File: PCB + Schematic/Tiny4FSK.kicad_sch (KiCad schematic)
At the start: 83 parts, among them J1 Power Ext, J2 GPIO, J3 I2C, J4 USB, J5 USB Breakout, J6 SPI, J7 USBC, J8 SWD, SW1 Power Switch, SW1 RST, U1 ATSAMD21G18A-A, U2 ATGM336H, U2 TPS61200DRC, U4 ECS-327TXO-2012, U6 SI4063, U7 Linear Step-Down

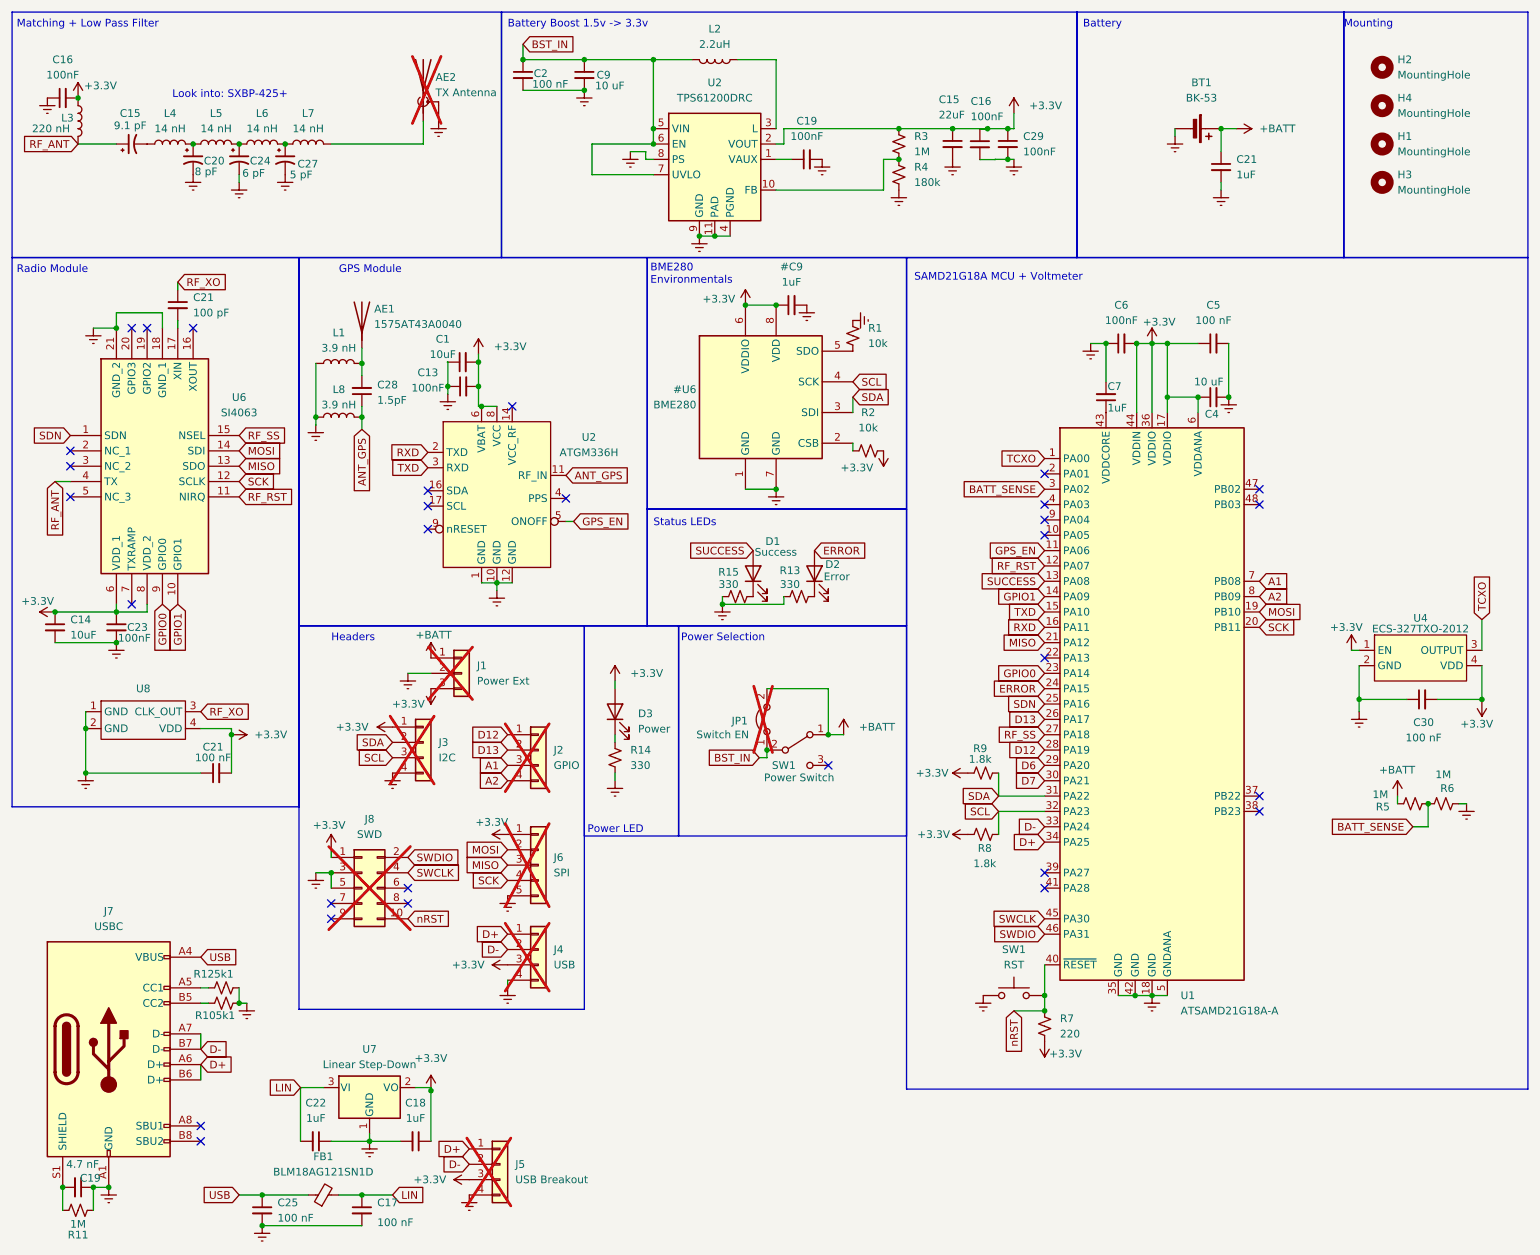
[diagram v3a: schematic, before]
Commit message: small updates to PCB, revamp README
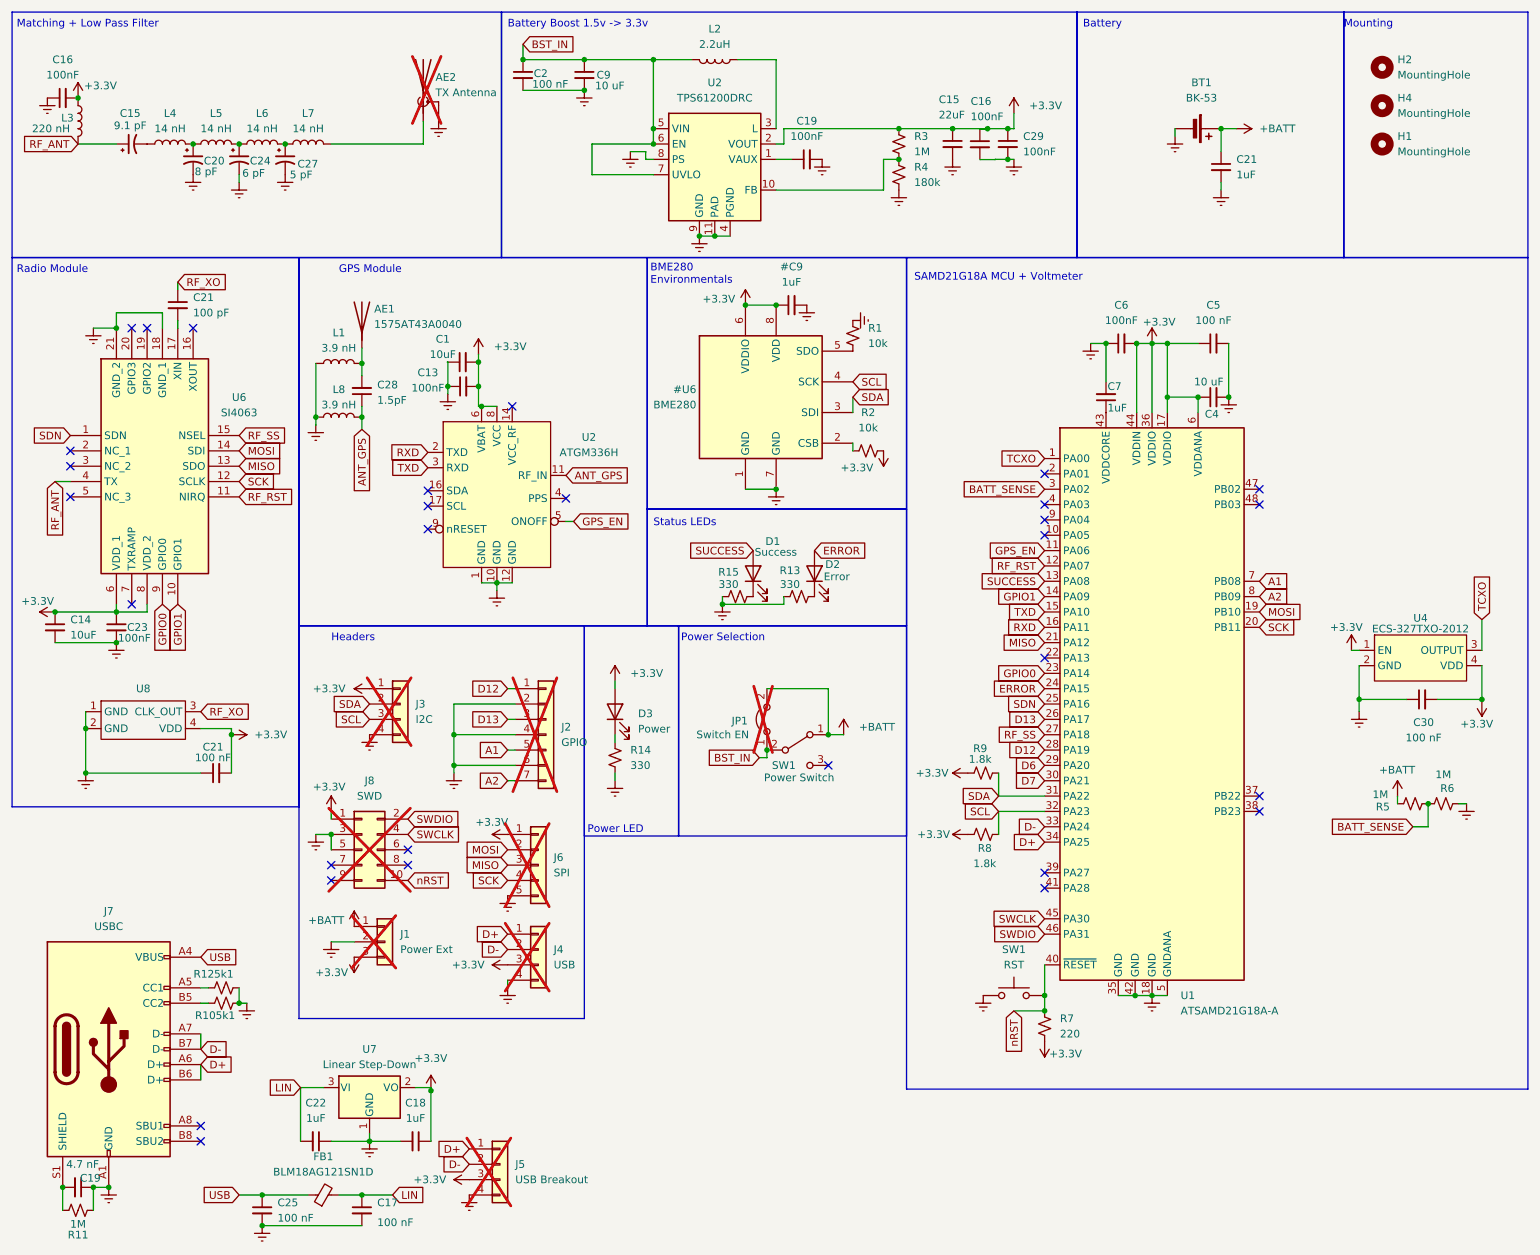
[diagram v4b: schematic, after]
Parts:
- removed H3: MountingHole, MountingHole:MountingHole_2.2mm_M2, symbol Mechanical:MountingHole
- removed J2: GPIO, Connector_PinHeader_2.54mm:PinHeader_1x04_P2.54mm_Vertical, symbol Connector_Generic:Conn_01x04
- added J2: GPIO, Connector_PinHeader_2.54mm:PinHeader_1x07_P2.54mm_Vertical, symbol Connector_Generic:Conn_01x07
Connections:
- net A1: now also J2.5 (Pin_5)
- net A2: now also J2.7 (Pin_7)
- net D12: now also J2.1 (Pin_1)
- net D13: now also J2.3 (Pin_3)
- net Earth: now also J2.2 (Pin_2), J2.4 (Pin_4), J2.6 (Pin_6)
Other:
- note removed: "Look into: SXBP-425+"
- moved on the sheet: J1, J3, J8

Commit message: Refactor Tiny4FSK project files and add shield functionality
- Updated Tiny4FSK.kicad_pro to include layer_pairs and changed the 3D model reference to Tiny4FSK-simple.step.
- Modified Tiny4FSK.kicad_sch to replace a 7-pin connector with a 9-pin connector, adjusting pin positions and properties accordingly.
- Introduced new shield.cpp and shield.h files to support interaction with the Tiny4FSK General Shield, including I2C scanning and initialization for BME280, IMU, and OLED devices.
- Added a new 3D model file Tiny4FSK-simple.step.
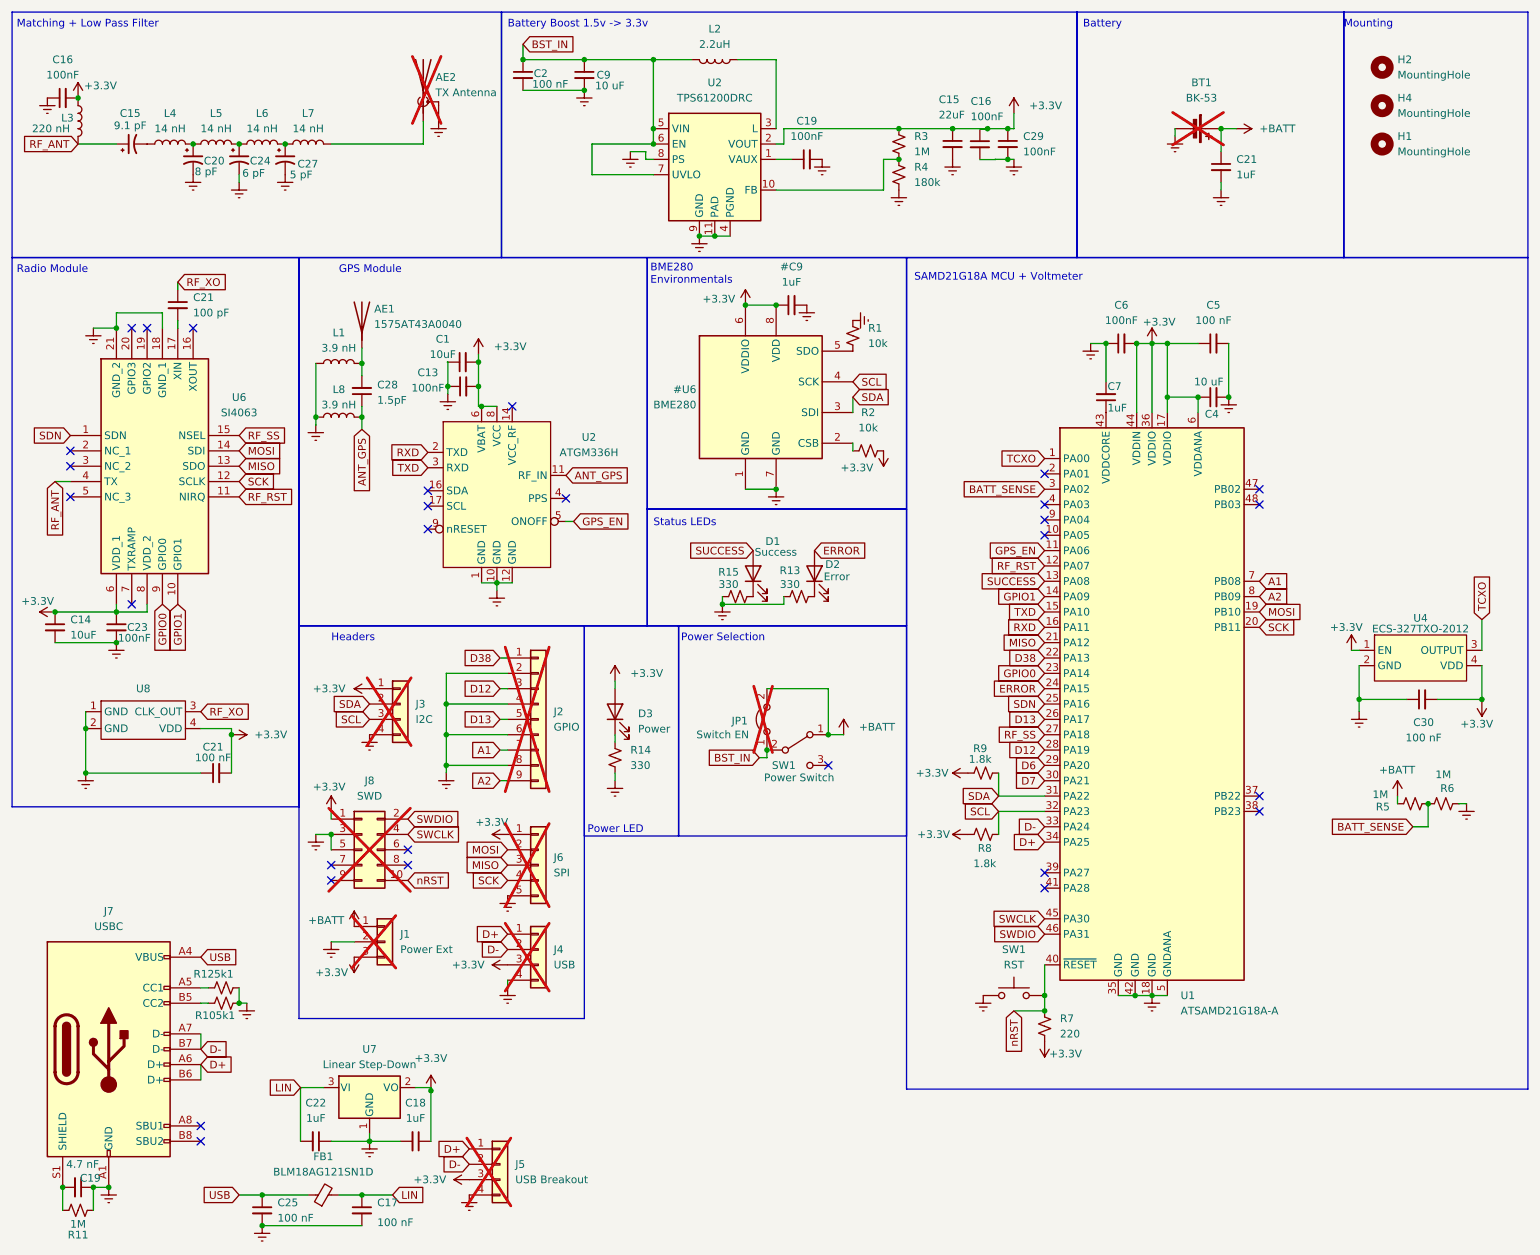
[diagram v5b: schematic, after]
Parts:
- BT1: now not fitted
- J2: footprint Connector_PinHeader_2.54mm:PinHeader_1x07_P2.54mm_Vertical -> Connector_PinHeader_2.54mm:PinHeader_1x09_P2.54mm_Vertical; symbol Connector_Generic:Conn_01x07 -> Connector_Generic:Conn_01x09
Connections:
- net A1: now also J2.7 (Pin_7); no longer J2.5 (Pin_5)
- net A2: now also J2.9 (Pin_9); no longer J2.7 (Pin_7)
- net D12: now also J2.3 (Pin_3); no longer J2.1 (Pin_1)
- net D13: now also J2.5 (Pin_5); no longer J2.3 (Pin_3)
- net Earth: now also J2.8 (Pin_8)
- net D38: now reaches U1.22 (PA13)
- net D38: now also J2.1 (Pin_1)
- no-connect marks 30 -> 29

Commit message: new production files
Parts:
- U4: footprint Oscillator_TCXO:ECS-327TXO-2012 -> Crystal:Crystal_SMD_3225-4Pin_3.2x2.5mm
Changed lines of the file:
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@@
 			)
 		)
-		(property "Footprint" "Oscillator_TCXO:ECS-327TXO-2012"
+		(property "Footprint" "Crystal:Crystal_SMD_3225-4Pin_3.2x2.5mm"
 			(at 247.65 118.11 0)
 			(effects

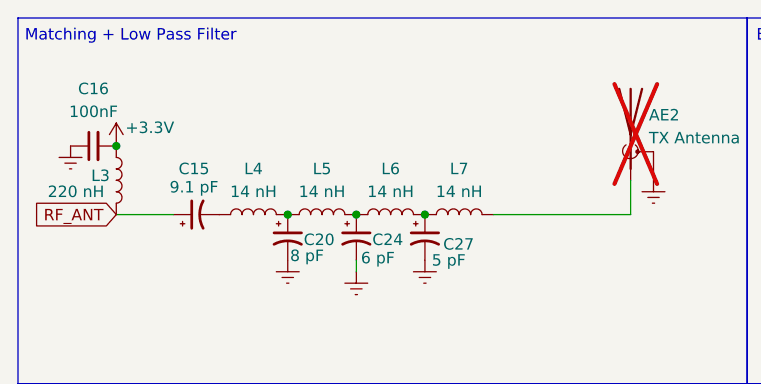
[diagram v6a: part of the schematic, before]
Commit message: add counterpoise to pcb
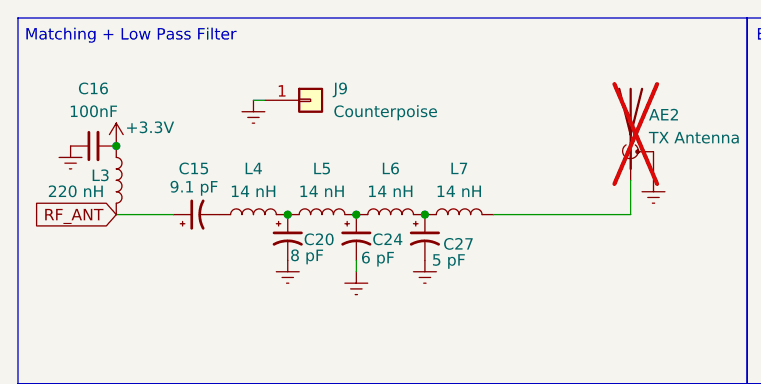
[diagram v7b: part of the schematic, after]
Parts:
- added J9: Counterpoise, Connector_PinHeader_2.54mm:PinHeader_1x01_P2.54mm_Vertical, symbol Connector_Generic:Conn_01x01
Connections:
- net Earth: now also J9.1 (Pin_1)
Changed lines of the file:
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@@
 	(wire
 		(pts
+			(xy 40.64 25.4) (xy 41.91 25.4)
+		)
+		(stroke
+			(width 0)
+			(type default)
+		)
+	)
+	(wire
+		(pts
 			(xy 67.31 152.4) (xy 67.31 154.94)
 		)
@@
 	)
 	(symbol
+		(lib_name "Earth_2")
+		(lib_id "power:Earth")
+		(at 40.64 25.4 0)
+		(unit 1)
+		(exclude_from_sim no)
+		(in_bom yes)
+		(on_board yes)
+		(dnp no)
+		(fields_autoplaced yes)
+		(property "Reference" "#PWR061"
+			(at 40.64 31.75 0)
+			(effects
+				(font
+					(size 1.27 1.27)
+				)
+				(hide yes)
+			)
+		)
+		(property "Value" "Earth"
+			(at 40.64 29.21 0)
+			(effects
+				(font
+					(size 1.27 1.27)
+				)
+				(hide yes)
+			)
+		)
+		(property "Footprint" ""
+			(at 40.64 25.4 0)
+			(effects
+				(font
+					(size 1.27 1.27)
+				)
+				(hide yes)
+			)
+		)
+		(property "Datasheet" "~"
+			(at 40.64 25.4 0)
+			(effects
+				(font
+					(size 1.27 1.27)
+				)
+				(hide yes)
+			)
+		)
+		(property "Description" ""
+			(at 40.64 25.4 0)
+			(effects
+				(font
+					(size 1.27 1.27)
+				)
+				(hide yes)
+			)
+		)
+		(pin "1"
+		)
+		(instances
+			(project "Tiny4FSK"
+				(path "/afd8b0bc-328a-481f-8ddf-c1252dc3b440"
+					(reference "#PWR061")
+					(unit 1)
+				)
+			)
+		)
+	)
+	(symbol
 		(lib_id "Device:LED")
 		(at 114.3 132.08 90)
@@
 					(unit 1)
 				)
+			)
+		)
+	)
+	(symbol
+		(lib_id "Connector_Generic:Conn_01x01")
+		(at 46.99 25.4 0)
+		(unit 1)
+		(exclude_from_sim no)
+		(in_bom yes)
+		(on_board yes)
+		(dnp no)
+		(fields_autoplaced yes)
+		(property "Reference" "J9"
+			(at 49.53 24.1299 0)
+			(effects
+				(font
+					(size 1.27 1.27)
+				)
+				(justify left)
+			)
+		)
+		(property "Value" "Counterpoise"
+			(at 49.53 26.6699 0)
+			(effects
+				(font
+					(size 1.27 1.27)
+				)
+				(justify left)
+			)
+		)
+		(property "Footprint" "Connector_PinHeader_2.54mm:PinHeader_1x01_P2.54mm_Vertical"
+			(at 46.99 25.4 0)
+			(effects
+				(font
+					(size 1.27 1.27)
+				)
+				(hide yes)
+			)
+		)
+		(property "Datasheet" "~"
+			(at 46.99 25.4 0)
+			(effects
+				(font
+					(size 1.27 1.27)
+				)
+				(hide yes)
+			)
+		)
+		(property "Description" "Generic connector, single row, 01x01, script generated (kicad-library-utils/schlib/autogen/connector/)"
+			(at 46.99 25.4 0)
+			(effects
+				(font
+					(size 1.27 1.27)
+				)
+				(hide yes)
+			)
+		)
+		(pin "1"
+		)
+		(instances
+			(project ""
+				(path "/afd8b0bc-328a-481f-8ddf-c1252dc3b440"
+					(reference "J9")
+					(unit 1)
+				)

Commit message: much better pics
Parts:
- renumbered C5 to C10, C7 to C11, C4 to C12, #C9 to C2, C21 to C26, C21 to C3, C15 to C4, C16 to C5, C2 to C6, C9 to C7, C19 to C8, C6 to C9, SW1 to SW2, #U6 to U1, U2 to U3, U1 to U5
